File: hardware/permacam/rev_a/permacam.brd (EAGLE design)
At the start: 27 x 60 mm, 109 parts, among them J1 TC2030-JLINK-NL, Q1 PMDXB950UPEL, Q2 PMDXB950UPEL, Q3 PMDXB950UPEL, Q4 PMDXB950UPEL, Q5 PMDXB950UPEL, Q6 PMDXB950UPEL, U1 AB1815-T3, U10 NRF52840, U2 BQ25505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

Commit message: Incorporate branden's suggestions
Add power switch, need to layout
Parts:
- added R8: 100k, passives:0402_RES
- added U9: TPS22860, chips:SOT-23-6
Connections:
- removed net N$16: C17.1, C18.1, C19.1, Q4.6, U4.12, U4.13, U4.14, U4.23, U4.8, U6.5
- new net CAM_EN: R8.2, U10.AC11, U9.6
- new net N$10: C18.1, U4.13, U4.14, U4.23
- new net N$13: C17.1, C19.1, Q4.6, U4.12, U4.8, U6.5, U9.1
- net GND: now also R8.1, U9.2
- net VCC: now also U9.4, U9.5
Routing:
- net N$16: track 55.8 -> 0.00 mm, vias 5 -> 0
- net N$13: track 0.00 -> 52.4 mm, vias 0 -> 5

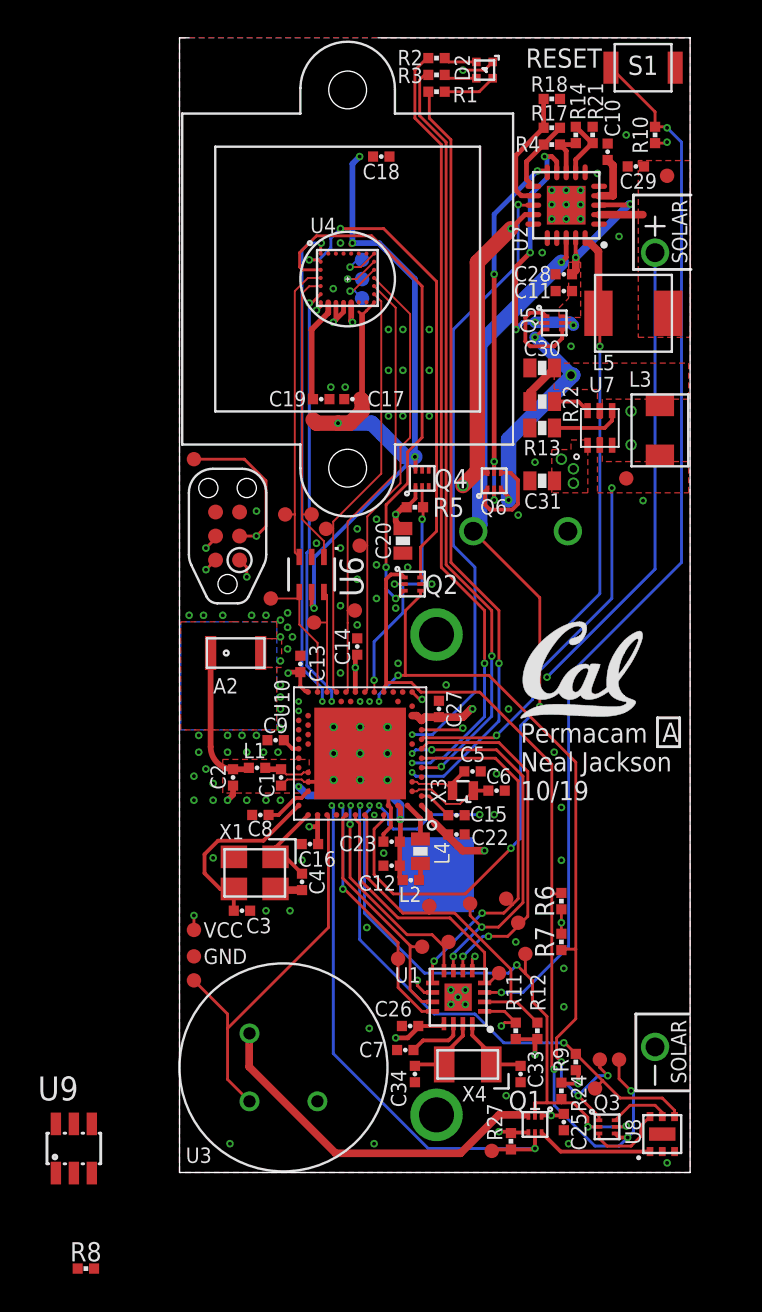
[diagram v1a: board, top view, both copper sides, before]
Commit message: Route power switch
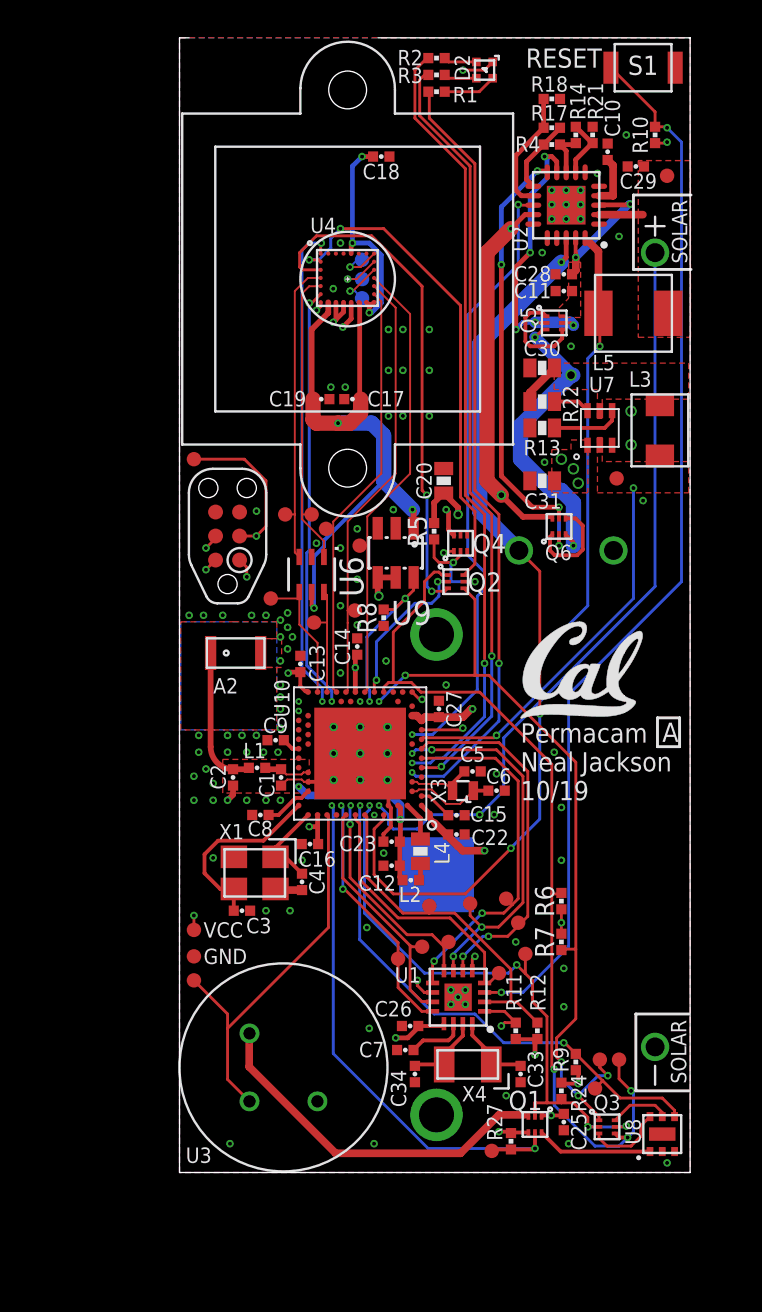
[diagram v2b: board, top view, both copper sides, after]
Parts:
- moved R8 37.8 mm to (10.8, 29.3), turned to 90 degrees
- moved U9 35.8 mm to (11.4, 32.8), turned to 180 degrees
- moved Q6 4.19 mm to (20.1, 34.2)
- moved Q4 3.99 mm to (14.9, 33.3)
- moved C20 3.84 mm to (14.0, 36.6), turned to 90 degrees
- moved BT1 2.62 mm to (20.4, 32.9)
- moved Q2 2.29 mm to (14.6, 31.2)
- moved R5 1.63 mm to (13.5, 33.9), turned to 90 degrees
- moved TP25 0.51 mm to (23.1, 36.7)
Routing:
- net N$13: track 52.4 -> 36.0 mm, vias 5 -> 4
- net N$10: track 0.00 -> 12.1 mm, vias 0 -> 3
- net CAM_EN: track 0.00 -> 9.03 mm, vias 1 -> 2
- net !VBAT_PRI_ON: track 20.1 -> 24.4 mm
- net VSW: track 14.8 -> 18.3 mm
- net VBAT: track 29.6 -> 33.0 mm
- net VCC: track 32.0 -> 34.9 mm, vias 19 -> 21
- net !CAM_EN: track 16.6 -> 14.8 mm
- net CAM_SCL: track 28.0 -> 27.1 mm
- net SDA: track 46.7 -> 47.4 mm
- net CAM_SDA: track 25.5 -> 26.1 mm
- net GND: track 21.8 -> 22.2 mm, vias 121 -> 115
- net VSOL: vias 3 -> 2

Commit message: update part numbers
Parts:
- removed C33, C34: DNP, passives:0402_CAP
- removed R21: 9.1M, passives:0402_RES
- removed R27: 100M, passives:0402_RES
- added C21: 1uF, passives:0402_CAP
- added C24: 4.7uF, passives:0402_CAP
- added R19, R20: DNP, passives:0402_RES
- C20: value 10uF -> 1uF; device passives:0603_CAP -> passives:0402_CAP
- C25, C26: value 1uF -> 4.7uF
- C27, C28, C29: value 4.7uF -> 10uF; device passives:0402_CAP -> passives:0603_CAP
- C30, C31: value 10uF -> DNP; device passives:0603_CAP -> passives:0402_CAP
- R10: value 10k -> 215k; device passives:0402_RES -> passives:0603-RES
- R11: value 10k -> 3.9M
- R12: value 10k -> 6.2M
- R13: value 215k -> 6.8M; device passives:0603-RES -> passives:0402_RES
- R14: value 3.9M -> 9.1M
- R17: value 6.2M -> 100M
- R18: value 6.8M -> 100M
- R5: value 100M -> 10k
- R6, R7: value DNP -> 10k
- R8: value 100k -> 10k
- R9: value 10k -> 100k
- moved R17 53.6 mm to (17.5, 1.65), turned to 90 degrees
- moved R12 47.8 mm to (19.7, 55.2), turned to 0 degrees
- moved R11 47.5 mm to (21.0, 54.9)
- moved C26 47.0 mm to (24.1, 53.2)
- moved C25 44.8 mm to (20.3, 47.5), turned to 180 degrees
- moved R6 40.8 mm to (25.1, 54.9)
- moved C30 37.4 mm to (18.0, 5.21), turned to 270 degrees
- moved C31 32.1 mm to (12.4, 5.21), turned to 270 degrees
- moved R5 29.0 mm to (21.0, 5.84), turned to 270 degrees
- moved R9 25.6 mm to (10.8, 29.3), turned to 90 degrees
- moved R18 23.7 mm to (13.5, 33.9), turned to 90 degrees
- moved R8 23.3 mm to (18.9, 7.49), turned to 270 degrees
- moved C29 19.5 mm to (14.0, 36.6), turned to 90 degrees
- moved C27 18.8 mm to (19.2, 42.5), turned to 180 degrees
- moved C20 18.7 mm to (14.6, 17.9), turned to 0 degrees
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- renumbered R22 to R15, R24 to R16
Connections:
- net !CAM_EN: now also R18.1; no longer R5.1
- net !LT_INT: now also R5.1; no longer R9.1
- net !PIR_EN: now also R17.1; no longer R27.1
- net !RST: now also R7.1; no longer R11.1
- net !RTC_EXTR: now also R6.1; no longer R10.1
- net CAM_EN: now also R9.2; no longer R8.2
- net GND: now also C21.2, C24.2, R10.1, R14.1, R9.1; no longer C33.2, C34.2, R18.1, R21.1, R8.1
- net N$12: now also R10.2; no longer R13.2
- net N$18: now also R11.1, R14.2; no longer R14.1, R21.2
- net N$26: now also C30.1; no longer C33.1
- net N$27: now also C31.1; no longer C34.1
- net N$3: now also C21.1; no longer C23.1
- net N$32: now also R11.2; no longer R14.2
- net N$57: now also R12.1, R13.2; no longer R17.1, R18.2
- net N$58: now also R12.2; no longer R17.2
- net SCL: now also R20.1; no longer R7.1
- net SDA: now also R19.1; no longer R6.1
- net VCC: now also C23.1, C24.1, C28.1, C29.1, R17.2, R18.2, R19.2, R20.2, R8.2; no longer C25.1, C26.1, C27.1, C31.1, R10.2, R11.2, R12.2, R27.2, R9.2
- net VOC_SAMP_VSTOR: now also C25.1; no longer C28.1
- net VSOL: now also C26.1; no longer C29.1
- net VSW: now also C27.1; no longer C30.1
- net WDI: now also R8.1; no longer R12.1
